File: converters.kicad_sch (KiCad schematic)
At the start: 23 parts, among them J1 USB_C_Receptacle, J2 DC 5V In, Q1 MMBT2222A-TP, U1 AP2112K-1.8, U2 TPS62160DSG, U9 USBLC6-2P6

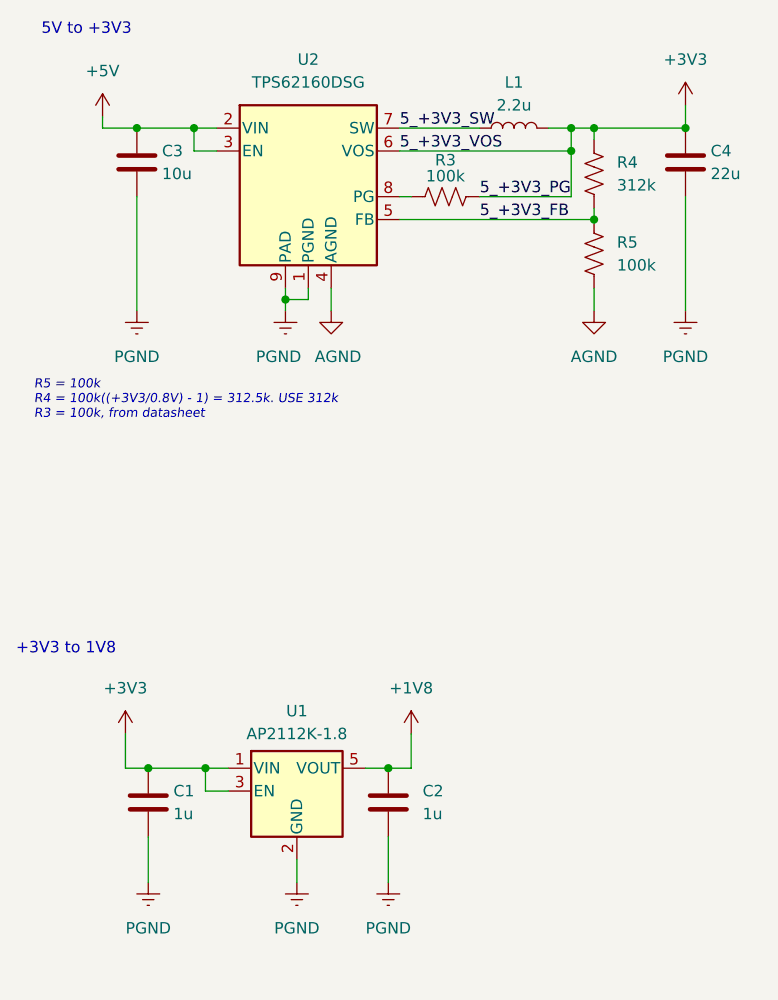
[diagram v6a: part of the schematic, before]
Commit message: Updated Schematics & finished rev2 layout. Routing left
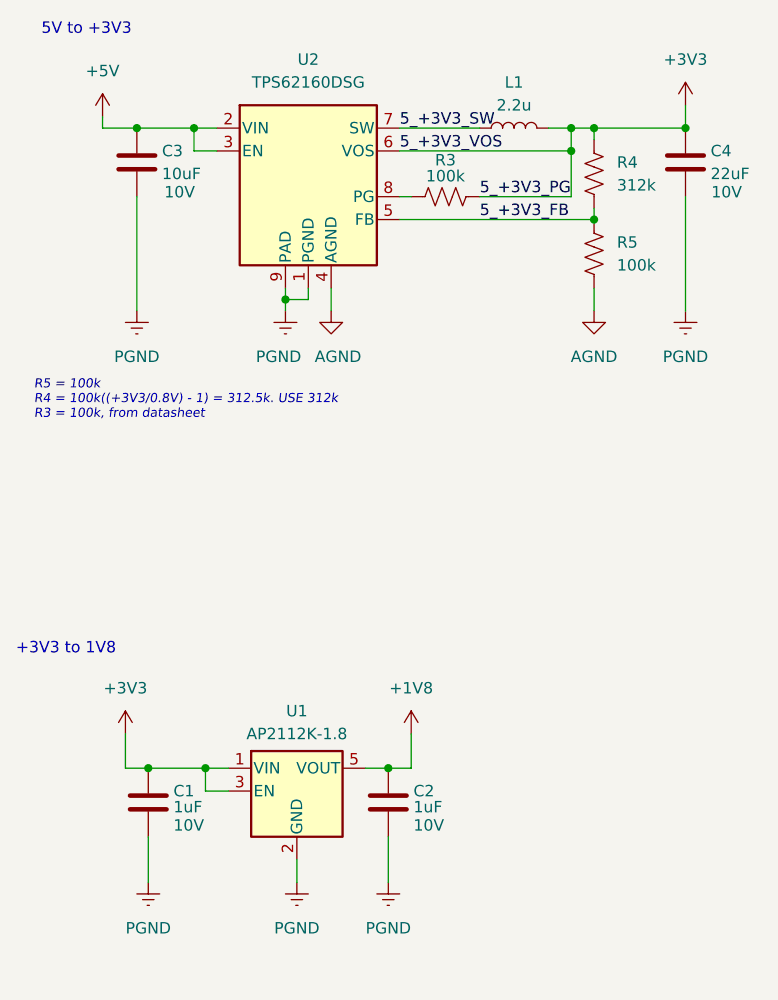
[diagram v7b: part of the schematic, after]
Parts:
- C1, C2: value 1u -> 1uF; footprint Capacitor_SMD:C_0805_2012Metric -> Capacitor_SMD:C_0603_1608Metric; Voltage Rating (none) -> 10V
- C3: value 10u -> 10uF; footprint Capacitor_SMD:C_0805_2012Metric -> Capacitor_SMD:C_0603_1608Metric; Voltage Rating (none) -> 10V
- C4: value 22u -> 22uF; footprint Capacitor_SMD:C_0805_2012Metric -> Capacitor_SMD:C_0603_1608Metric; Voltage Rating (none) -> 10V
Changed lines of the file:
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@@
 	)
 	(junction
+		(at 151.13 124.46)
+		(diameter 0)
+		(color 0 0 0 0)
+	)
+	(junction
 		(at 130.81 124.46)
 		(diameter 0)
@@
 		(color 0 0 0 0)
 	)
-	(junction
-		(at 151.13 124.46)
-		(diameter 0)
-		(color 0 0 0 0)
-	)
 	(no_connect
 		(at 49.53 69.85)
@@
 	(wire
 		(pts
-			(xy 151.13 124.46) (xy 153.67 124.46)
+			(xy 173.99 63.5) (xy 173.99 62.23)
 		)
 		(stroke
@@
 	(wire
 		(pts
-			(xy 173.99 63.5) (xy 173.99 62.23)
+			(xy 144.78 71.12) (xy 144.78 73.66)
 		)
 		(stroke
@@
 	(wire
 		(pts
-			(xy 144.78 71.12) (xy 144.78 73.66)
+			(xy 123.19 53.34) (xy 129.54 53.34)
 		)
 		(stroke
@@
 	(wire
 		(pts
-			(xy 123.19 53.34) (xy 129.54 53.34)
+			(xy 123.19 60.96) (xy 123.19 73.66)
 		)
 		(stroke
@@
 	(wire
 		(pts
-			(xy 123.19 60.96) (xy 123.19 73.66)
+			(xy 151.13 124.46) (xy 153.67 124.46)
 		)
 		(stroke
@@
 	)
 	(symbol
+		(lib_id "Device:C")
+		(at 151.13 128.27 0)
+		(unit 1)
+		(body_style 1)
+		(exclude_from_sim no)
+		(in_bom yes)
+		(on_board yes)
+		(in_pos_files yes)
+		(dnp no)
+		(property "Reference" "C2"
+			(at 153.924 127 0)
+			(show_name no)
+			(do_not_autoplace no)
+			(effects
+				(font
+					(size 1.27 1.27)
+				)
+				(justify left)
+			)
+		)
+		(property "Value" "1uF"
+			(at 153.924 128.778 0)
+			(show_name no)
+			(do_not_autoplace no)
+			(effects
+				(font
+					(size 1.27 1.27)
+				)
+				(justify left)
+			)
+		)
+		(property "Footprint" "Capacitor_SMD:C_0603_1608Metric"
+			(at 152.0952 132.08 0)
+			(hide yes)
+			(show_name no)
+			(do_not_autoplace no)
+			(effects
+				(font
+					(size 1.27 1.27)
+				)
+			)
+		)
+		(property "Datasheet" ""
+			(at 151.13 128.27 0)
+			(hide yes)
+			(show_name no)
+			(do_not_autoplace no)
+			(effects
+				(font
+					(size 1.27 1.27)
+				)
+			)
+		)
+		(property "Description" "Unpolarized capacitor"
+			(at 151.13 128.27 0)
+			(hide yes)
+			(show_name no)
+			(do_not_autoplace no)
+			(effects
+				(font
+					(size 1.27 1.27)
+				)
+			)
+		)
+		(property "Voltage Rating" "10V"
+			(at 153.924 130.81 0)
+			(show_name no)
+			(do_not_autoplace no)
+			(effects
+				(font
+					(size 1.27 1.27)
+				)
+				(justify left)
+			)
+		)
+		(pin "2"
+		)
+		(pin "1"
+		)
+		(instances
+			(project "Telemetry Box"
+				(path "/71a96c1a-3810-48e8-8b77-829a22b612db/e1044467-df55-4773-adfc-6bc275c0743b"
+					(reference "C2")
+					(unit 1)
+				)
+			)
+		)
+	)
+	(symbol
 		(lib_id "power:Earth")
 		(at 124.46 137.16 0)
@@
 			)
 		)
-		(property "Value" "1u"
-			(at 127.254 129.54 0)
+		(property "Value" "1uF"
+			(at 127.254 128.778 0)
 			(show_name no)
 			(do_not_autoplace no)
@@
 			)
 		)
-		(property "Footprint" "Capacitor_SMD:C_0805_2012Metric"
+		(property "Footprint" "Capacitor_SMD:C_0603_1608Metric"
 			(at 125.4252 132.08 0)
 			(hide yes)
@@
 			)
 		)
+		(property "Voltage Rating" "10V"
+			(at 127.254 130.81 0)
+			(show_name no)
+			(do_not_autoplace no)
+			(effects
+				(font
+					(size 1.27 1.27)
+				)
+				(justify left)
+			)
+		)
 		(pin "2"
 		)
@@
 			)
 		)
-		(property "Value" "10u"
+		(property "Value" "10uF"
 			(at 125.984 58.42 0)
 			(show_name no)
@@
 			)
 		)
-		(property "Footprint" "Capacitor_SMD:C_0805_2012Metric"
+		(property "Footprint" "Capacitor_SMD:C_0603_1608Metric"
 			(at 124.1552 60.96 0)
 			(hide yes)
@@
 			)
 		)
+		(property "Voltage Rating" "10V"
+			(at 126.238 60.452 0)
+			(show_name no)
+			(do_not_autoplace no)
+			(effects
+				(font
+					(size 1.27 1.27)
+				)
+				(justify left)
+			)
+		)
 		(pin "2"
 		)
@@
 			)
 		)
-		(property "Value" "22u"
+		(property "Value" "22uF"
 			(at 186.944 58.42 0)
 			(show_name no)
@@
 			)
 		)
-		(property "Footprint" "Capacitor_SMD:C_0805_2012Metric"
+		(property "Footprint" "Capacitor_SMD:C_0603_1608Metric"
 			(at 185.1152 60.96 0)
 			(hide yes)
@@
 			)
 		)
+		(property "Voltage Rating" "10V"
+			(at 188.722 60.452 0)
+			(show_name no)
+			(do_not_autoplace no)
+			(effects
+				(font
+					(size 1.27 1.27)
+				)
+			)
+		)
 		(pin "2"
 		)
@@
 					(unit 1)
 				)
-			)
-		)
-	)
-	(symbol
-		(lib_id "Device:C")
-		(at 151.13 128.27 0)
-		(unit 1)
-		(body_style 1)
-		(exclude_from_sim no)
-		(in_bom yes)
-		(on_board yes)
-		(in_pos_files yes)
-		(dnp no)
-		(fields_autoplaced yes)
-		(property "Reference" "C2"
-			(at 154.94 126.9999 0)
-			(show_name no)
-			(do_not_autoplace no)
-			(effects
-				(font
-					(size 1.27 1.27)
-				)
-				(justify left)
-			)
-		)
-		(property "Value" "1u"
-			(at 154.94 129.5399 0)
-			(show_name no)
-			(do_not_autoplace no)
-			(effects
-				(font
-					(size 1.27 1.27)
-				)
-				(justify left)
-			)
-		)
-		(property "Footprint" "Capacitor_SMD:C_0805_2012Metric"
-			(at 152.0952 132.08 0)
-			(hide yes)
-			(show_name no)
-			(do_not_autoplace no)
-			(effects
-				(font
-					(size 1.27 1.27)
-				)
-			)
-		)
-		(property "Datasheet" ""
-			(at 151.13 128.27 0)
-			(hide yes)
-			(show_name no)
-			(do_not_autoplace no)
-			(effects
-				(font
-					(size 1.27 1.27)
-				)
-			)
-		)
-		(property "Description" "Unpolarized capacitor"
-			(at 151.13 128.27 0)
-			(hide yes)
-			(show_name no)
-			(do_not_autoplace no)
-			(effects
-				(font
-					(size 1.27 1.27)
-				)
-			)
-		)
-		(pin "2"
-		)
-		(pin "1"
-		)
-		(instances
-			(project "Telemetry Box"
-				(path "/71a96c1a-3810-48e8-8b77-829a22b612db/e1044467-df55-4773-adfc-6bc275c0743b"
-					(reference "C2")
-					(unit 1)
-				)
